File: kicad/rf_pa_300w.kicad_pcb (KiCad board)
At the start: 2 copper layers, 80 x 50 mm, 21 parts, among them J1 Vdd 72.5V, J2 SMA 50ohm, J3 VCC 12V, J4 PWM IN, Q1 IRF540, Q2 IRF540, U1 IR2181S

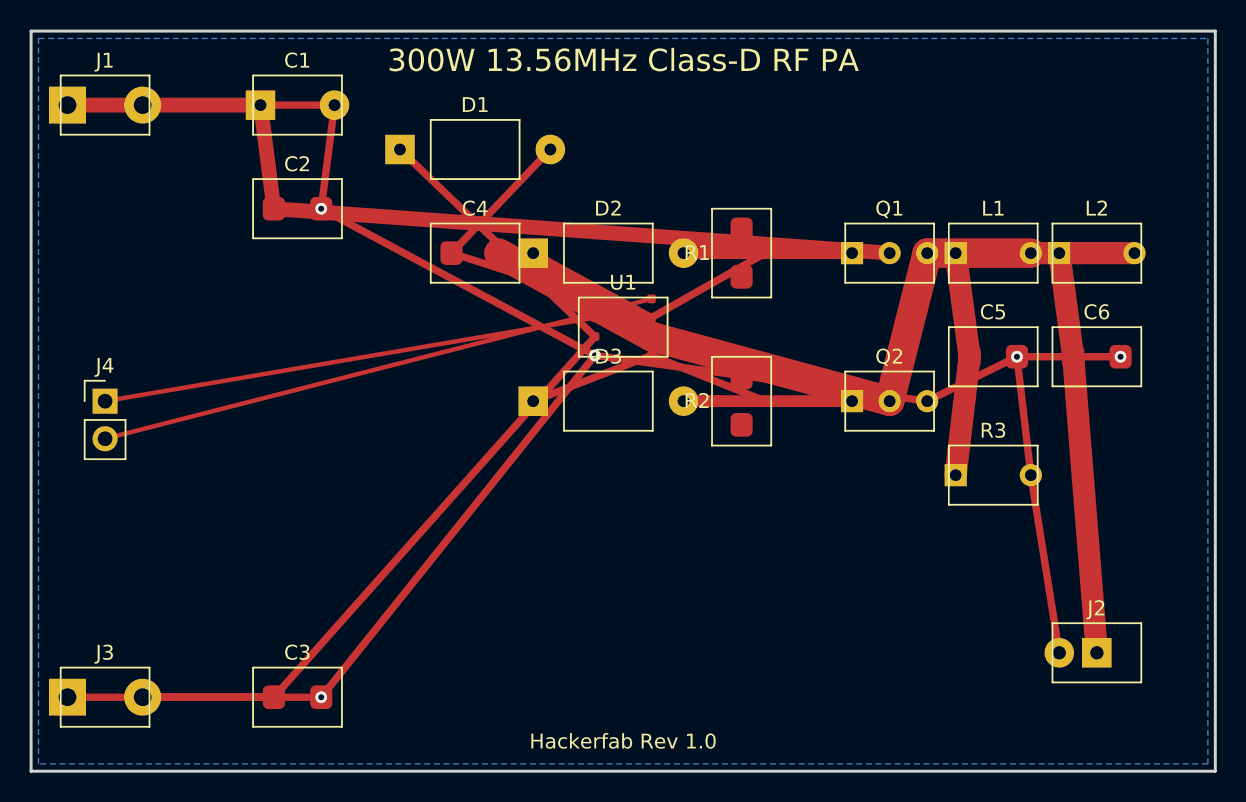
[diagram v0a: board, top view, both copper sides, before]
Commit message: Complete schematic wiring, PCB trace routing, DRC/ERC validation, and Gerber generation
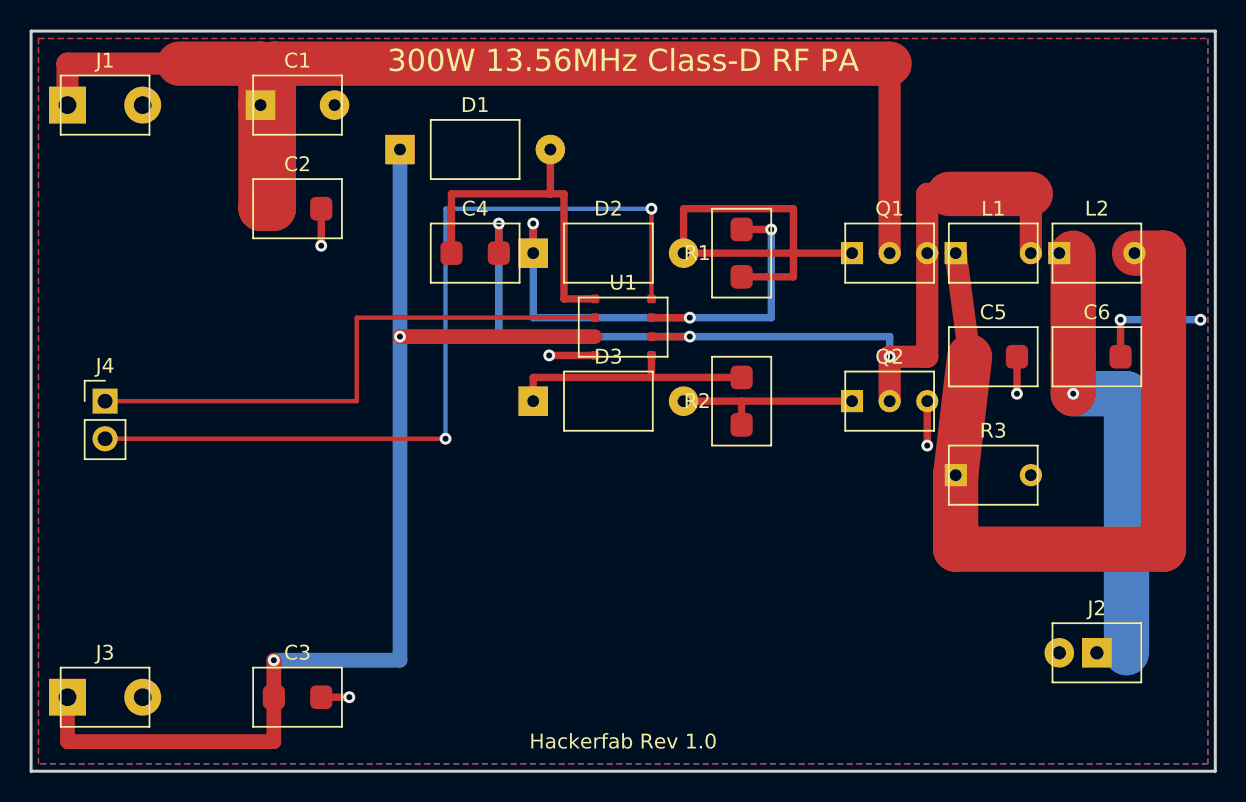
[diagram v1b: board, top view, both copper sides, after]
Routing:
- net GND: track 139.3 -> 20.9 mm, vias 5 -> 7
- net +72V5: track 61.8 -> 90.7 mm
- net /TANK_OUT: track 27.2 -> 56.1 mm
- net /MID: track 45.7 -> 67.5 mm, vias 0 -> 3
- net /LIN: track 38.1 -> 58.5 mm, vias 0 -> 2
- net /GATE1: track 11.4 -> 29.9 mm
- net /HO_NET: track 17.9 -> 35.0 mm, vias 0 -> 3
- net VCC: track 64.8 -> 78.6 mm, vias 0 -> 2
- net /RF_OUT: track 27.1 -> 33.5 mm, vias 0 -> 1
- net /HIN: track 33.6 -> 38.7 mm
- net VB: track 19.8 -> 23.8 mm
- net /GATE2: track 11.4 -> 13.0 mm
- added copper zone on F.Cu, net GND
